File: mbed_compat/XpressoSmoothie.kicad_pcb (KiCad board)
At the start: 2 copper layers, 99.7 x 99.7 mm, 122 parts, among them J1 HEADER_4, J10 HEADER_3X2, J11 Pwr_in, J12 HEADER_4, J13 HEADER_4X2, J14 HEADER_3X2, J15 HEADER_4, J16 HEADER_3, J17 HEADER_3, J18 HEADER_3, J19 HEADER_2, J2 HEADER_4, J20 HEADER_2, J21 HEADER_2, J22 HEADER_2, J23 HEADER_3, J24 HEADER_3, J25 HEADER_3, J26 USB, J27 HEADER_4, J28 MICROSD-MOLEX, J3 HEADER_3, J4 HEADER_3X2, J5 HEADER_3X2, J6 LPCXPRESSO_GENERIC_HEADER, J7 HEADER_4, J8 HEADER_4, J9 HEADER_3X2, M1 LOGO_OSHW, M2 LOGO_OSHW, Q1 IRLB 8743, Q2 IRLB 8743, Q3 IRLB 8743, Q4 IRLB 8743, SW1 SW_PUSH, SW2 SW_PUSH, U1 POLOLU_A4988, U10 TC4422A, U11 TC4422A, U12 LM1117-3.3, U2 POLOLU_A4988, U3 POLOLU_A4988, U4 POLOLU_A4988, U5 POLOLU_A4988, U7 LM7812CT, U8 TC4422A, U9 TC4422A

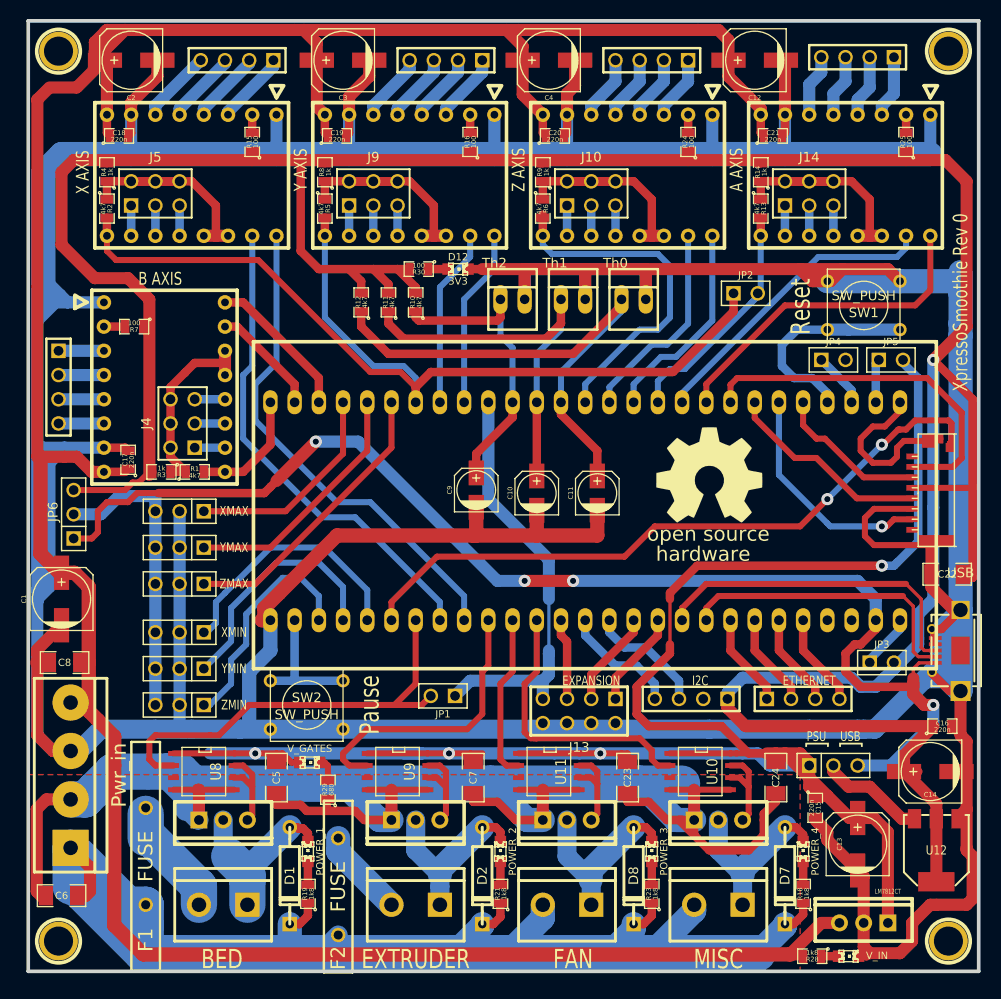
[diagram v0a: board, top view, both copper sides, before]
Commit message: endstops 4 pins
endstops 4 pins, removed jumper selector
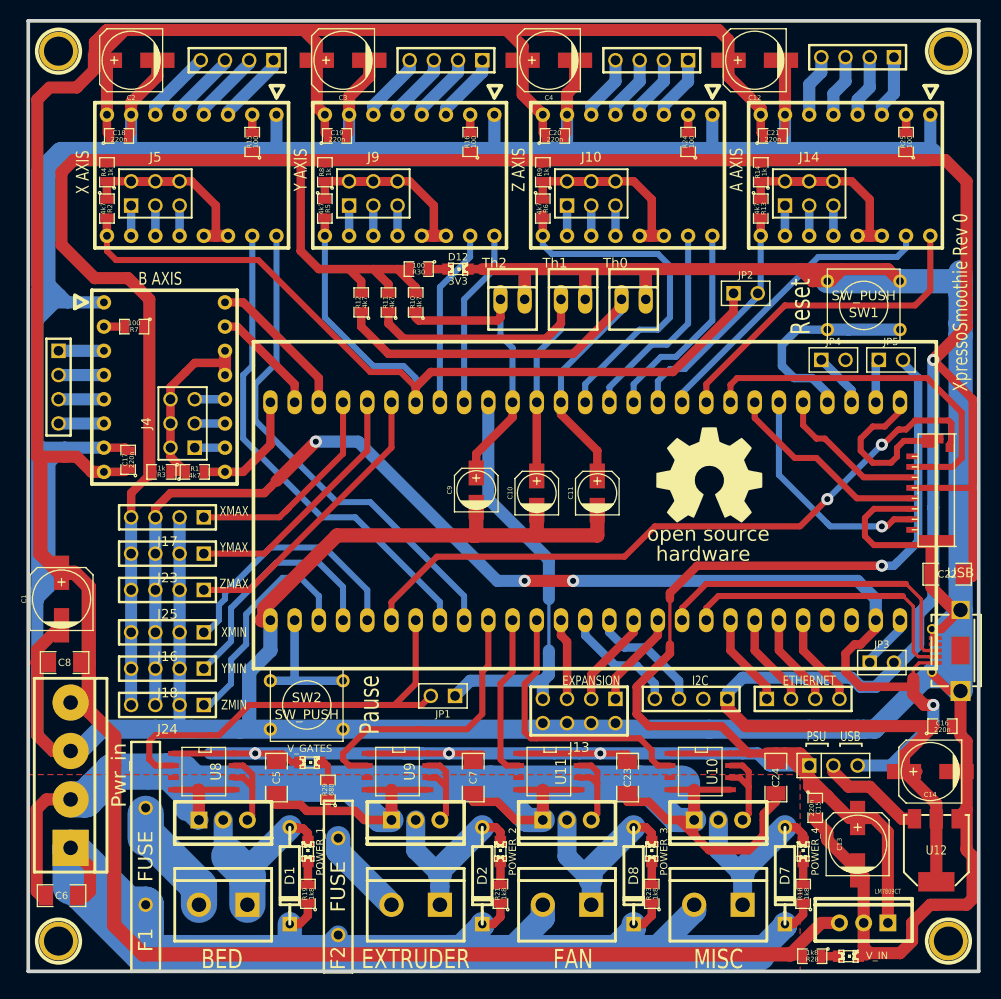
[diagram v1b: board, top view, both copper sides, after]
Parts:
- removed JP6: JUMPER-3, PIN_ARRAY_3X1
- J16, J17, J18, J23, J24, J25: value HEADER_3 -> HEADER_4; footprint PIN_ARRAY_3X1 -> PIN_ARRAY_4x1
- U7: value LM7812CT -> LM7809CT
- moved J17 1.42 mm to (86.4, 106.0)
- moved J23 1.42 mm to (86.4, 109.9)
- moved J25 1.42 mm to (86.4, 113.7)
- moved J16 1.27 mm to (86.4, 118.1)
- moved J18 1.27 mm to (86.4, 121.9)
- moved J24 1.27 mm to (86.4, 125.7)
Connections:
- J16 pad 3: /E+ -> +5V
- J17 pad 3: /E+ -> +5V
- J18 pad 3: /E+ -> +5V
- J23 pad 3: /E+ -> +5V
- J24 pad 3: /E+ -> +5V
- J25 pad 3: /E+ -> +5V
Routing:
- net /E+: track 31.3 -> 0.00 mm
- net +3.3VP: track 336.8 -> 353.5 mm
- net +5V: track 133.0 -> 142.5 mm
- net XMAX: track 22.5 -> 23.2 mm
- net GND: track 759.7 -> 759.1 mm
